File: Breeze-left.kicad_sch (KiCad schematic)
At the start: 102 parts, among them SW1 CHOCXHSPCB-1U, SW10 CHOCXHSPCB-1U, SW11 CHOCXHSPCB-1U, SW12 CHOCXHSPCB-1U, SW13 CHOCXHSPCB-1U, SW14 CHOCXHSPCB-1U, SW15 CHOCXHSPCB-1U, SW16 CHOCXHSPCB-1U, SW17 CHOCXHSPCB-1U, SW18 CHOCXHSPCB-1U, SW19 CHOCXHSPCB-1U, SW2 CHOCXHSPCB-1U, SW20 CHOCXHSPCB-1U, SW21 CHOCXHSPCB-1U, SW22 CHOCXHSPCB-1U, SW23 CHOCXHSPCB-1U, SW24 CHOCXHSPCB-1U, SW3 CHOCXHSPCB-1U, SW4 CHOCXHSPCB-1U, SW5 CHOCXHSPCB-1U, SW6 CHOCXHSPCB-1U, SW7 CHOCXHSPCB-1U, SW8 CHOCXHSPCB-1U, SW9 CHOCXHSPCB-1U

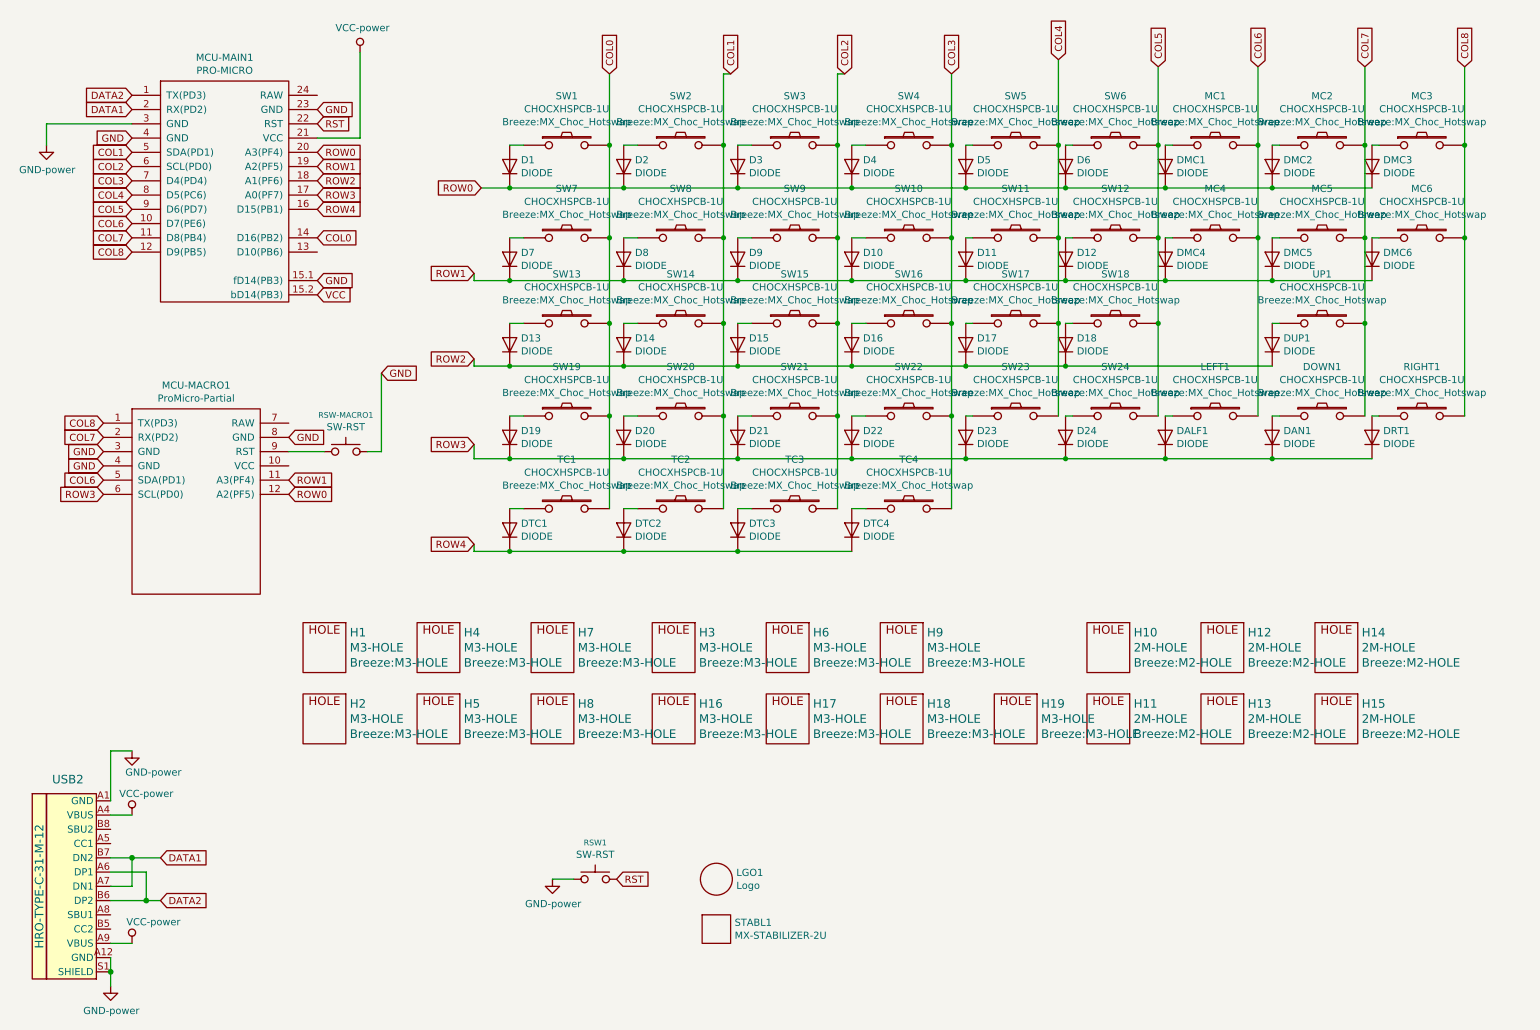
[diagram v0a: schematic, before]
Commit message: Copy right half to left
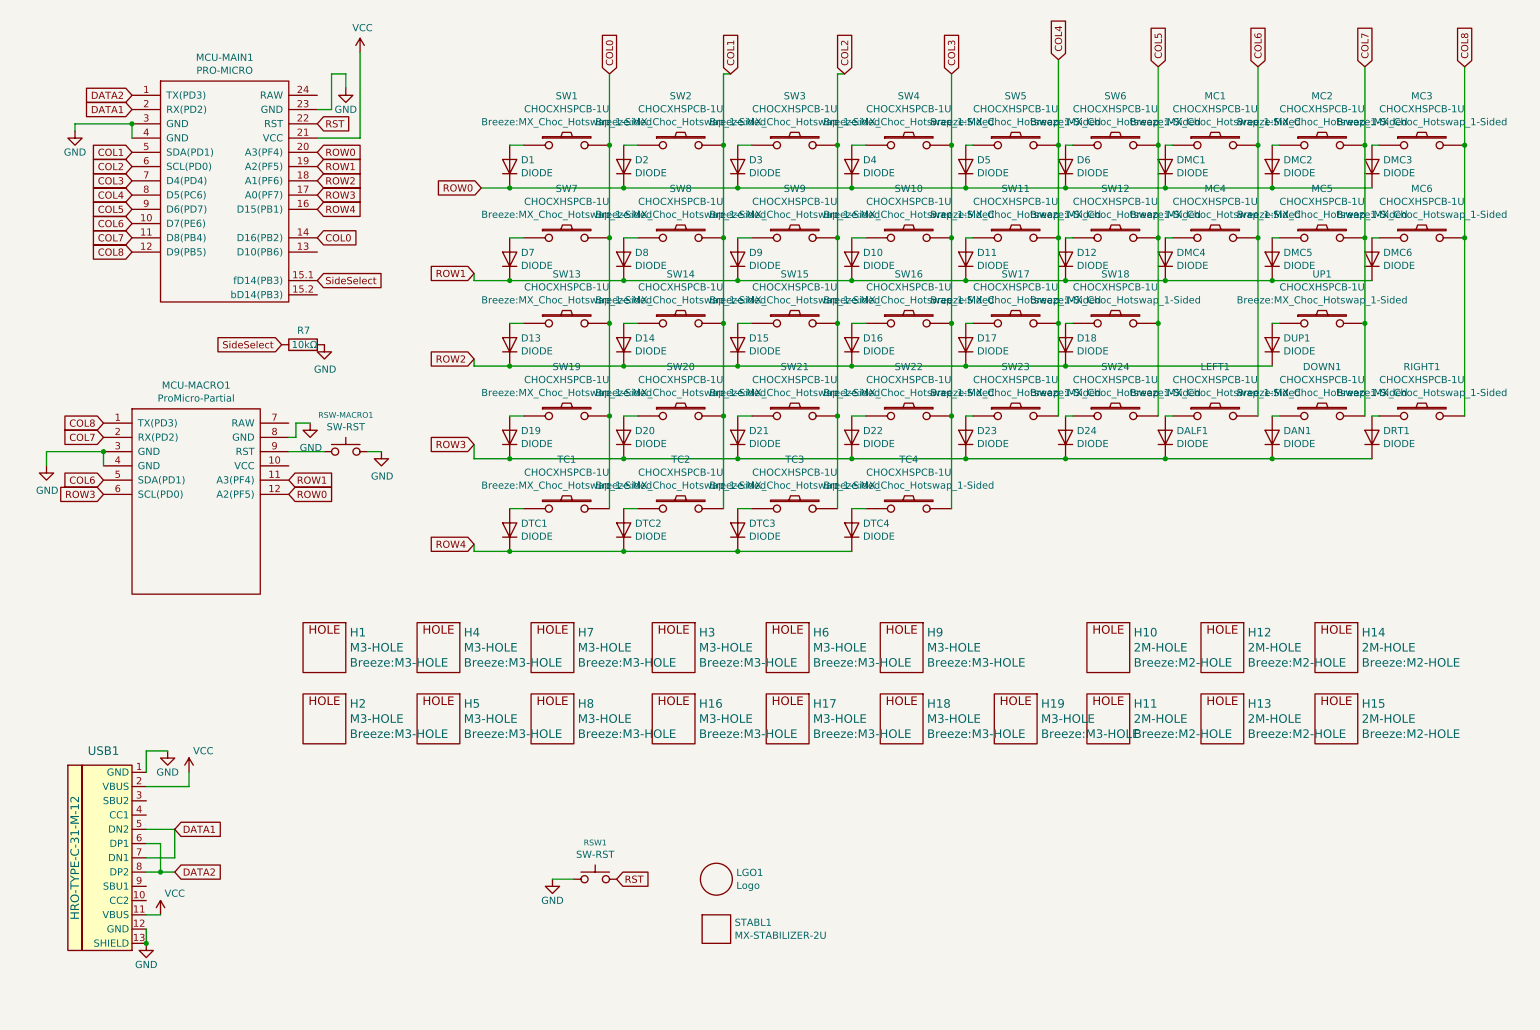
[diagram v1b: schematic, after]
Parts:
- removed USB2: HRO-TYPE-C-31-M-12, Connector_USB:USB_C_Receptacle_HRO_TYPE-C-31-M-12, symbol keebio:HRO-TYPE-C-31-M-12
- added R7: 10kΩ, Resistor_SMD:R_0603_1608Metric, symbol Device:R
- added USB1: HRO-TYPE-C-31-M-12, Keebio-Parts:USB-C-12-Pin-MidMount, symbol keebio:HRO-TYPE-C-31-M-12
- DOWN1, LEFT1, MC1, MC2, MC3, MC4, MC5, MC6, RIGHT1, SW1, SW10, SW11, SW12, SW13, SW14, SW15, SW16, SW17, SW18, SW19, SW2, SW20, SW21, SW22, SW23, SW24, SW3, SW4, SW5, SW6, SW7, SW8, SW9, TC1, TC2, TC3, TC4, UP1: footprint Breeze:MX_Choc_Hotswap -> Breeze:MX_Choc_Hotswap_1-Sided
- MCU-MAIN1: footprint Breeze:ProMicro -> Breeze:ProMicro_1-Sided
- RSW-MACRO1: footprint Breeze:TACT_SWITCH_TVBP06 -> Button_Switch_SMD:SW_SPST_TL3342
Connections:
- net DATA1: now also USB1.5 (DN2), USB1.7 (DN1)
- net DATA2: now also USB1.6 (DP1), USB1.8 (DP2)
- net GND: now also R7.2, USB1.1 (GND), USB1.12 (GND), USB1.13 (SHIELD); no longer MCU-MAIN1.15.1 (fD14(PB3))
- net VCC: now also USB1.11 (VBUS), USB1.2 (VBUS); no longer MCU-MAIN1.15.2 (bD14(PB3))
- new net SideSelect: MCU-MAIN1.15.1 (fD14(PB3)), R7.1

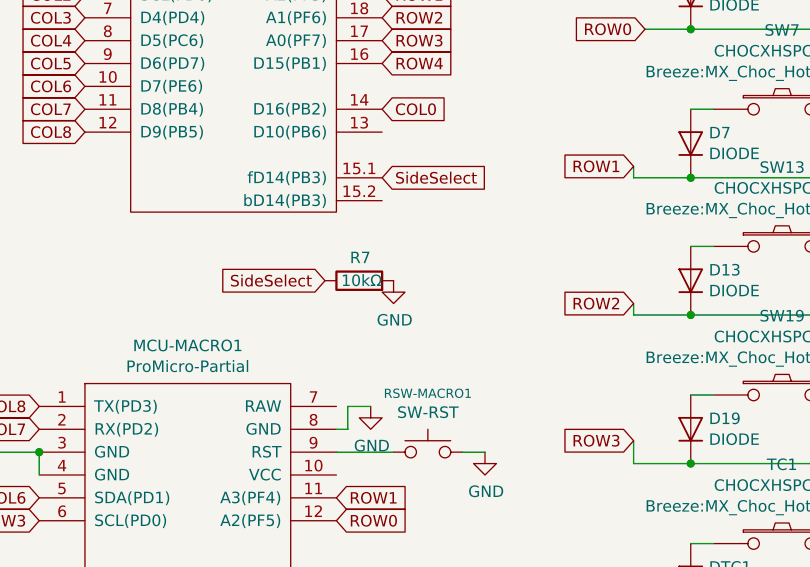
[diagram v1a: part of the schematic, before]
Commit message: Set side select config for left half
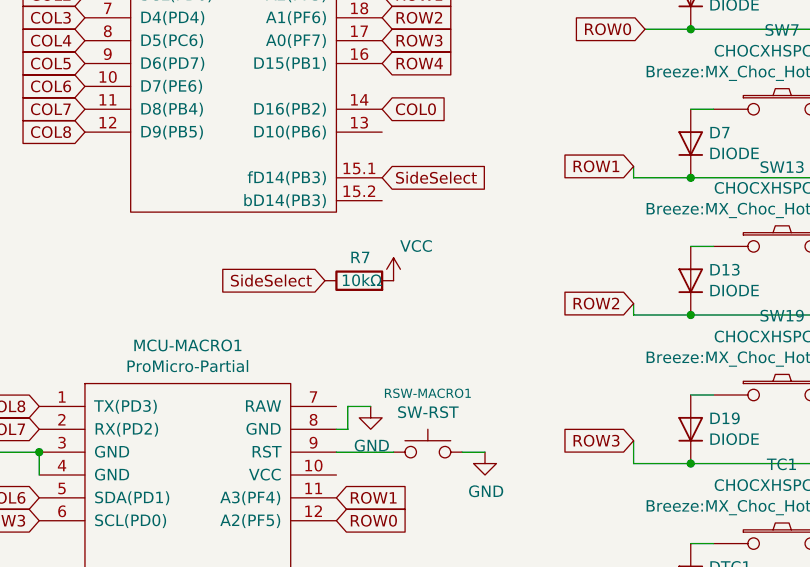
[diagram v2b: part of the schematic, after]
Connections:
- net GND: no longer R7.2
- net VCC: now also R7.2

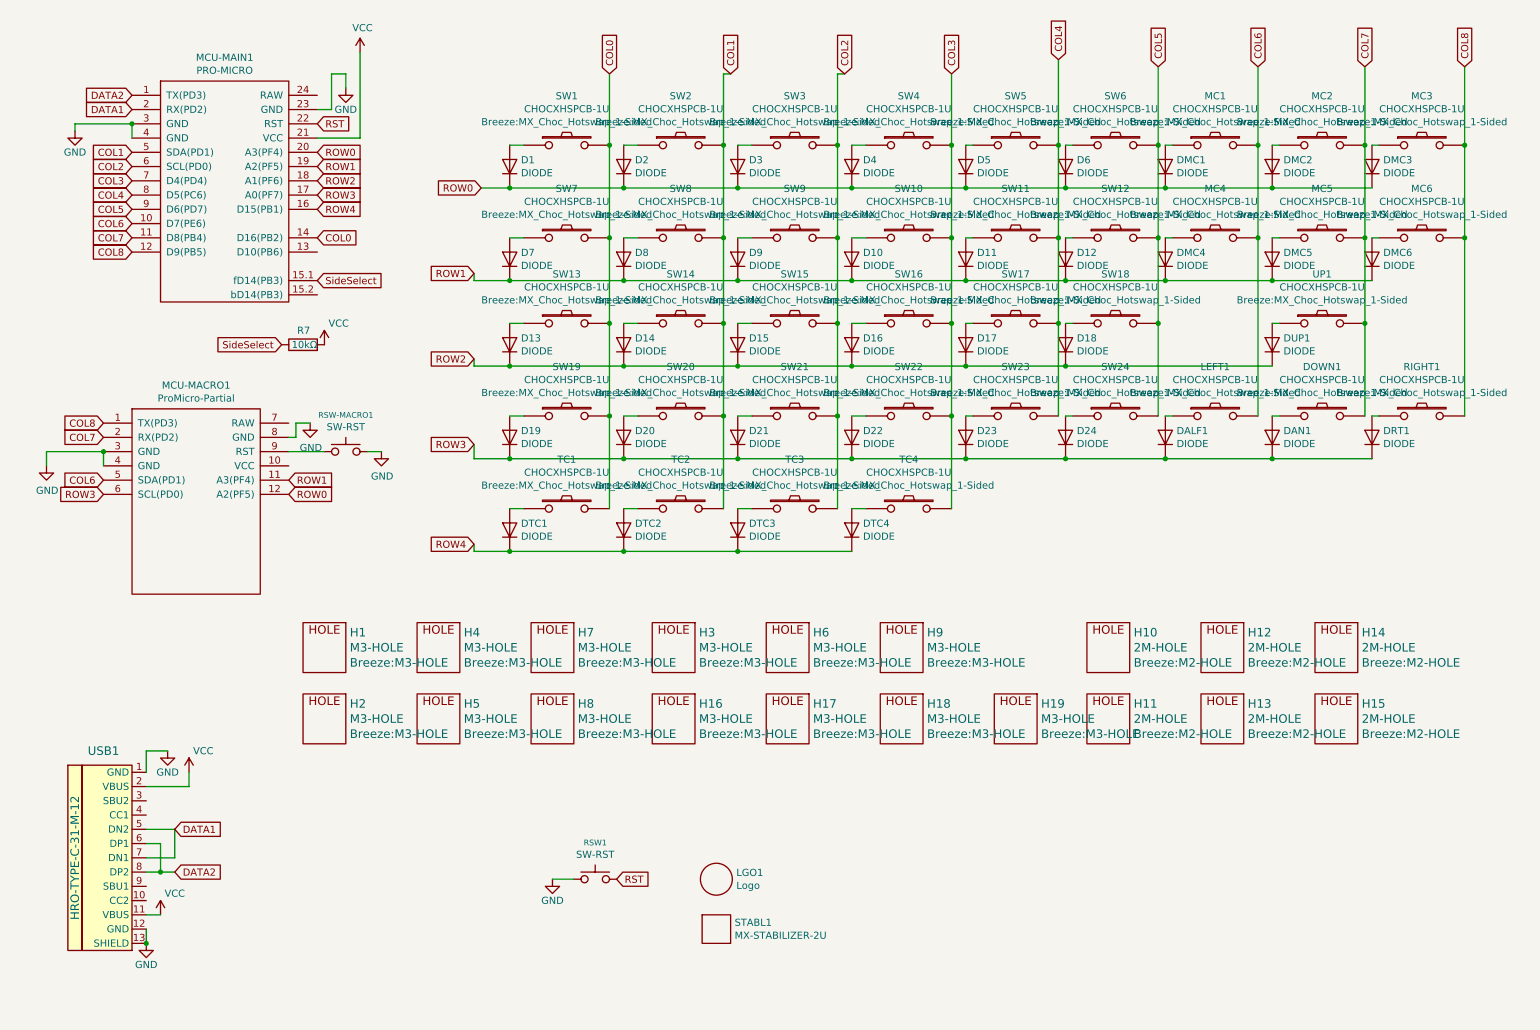
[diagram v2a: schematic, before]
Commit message: Remove extra holes and switches for breakoff portion on left half
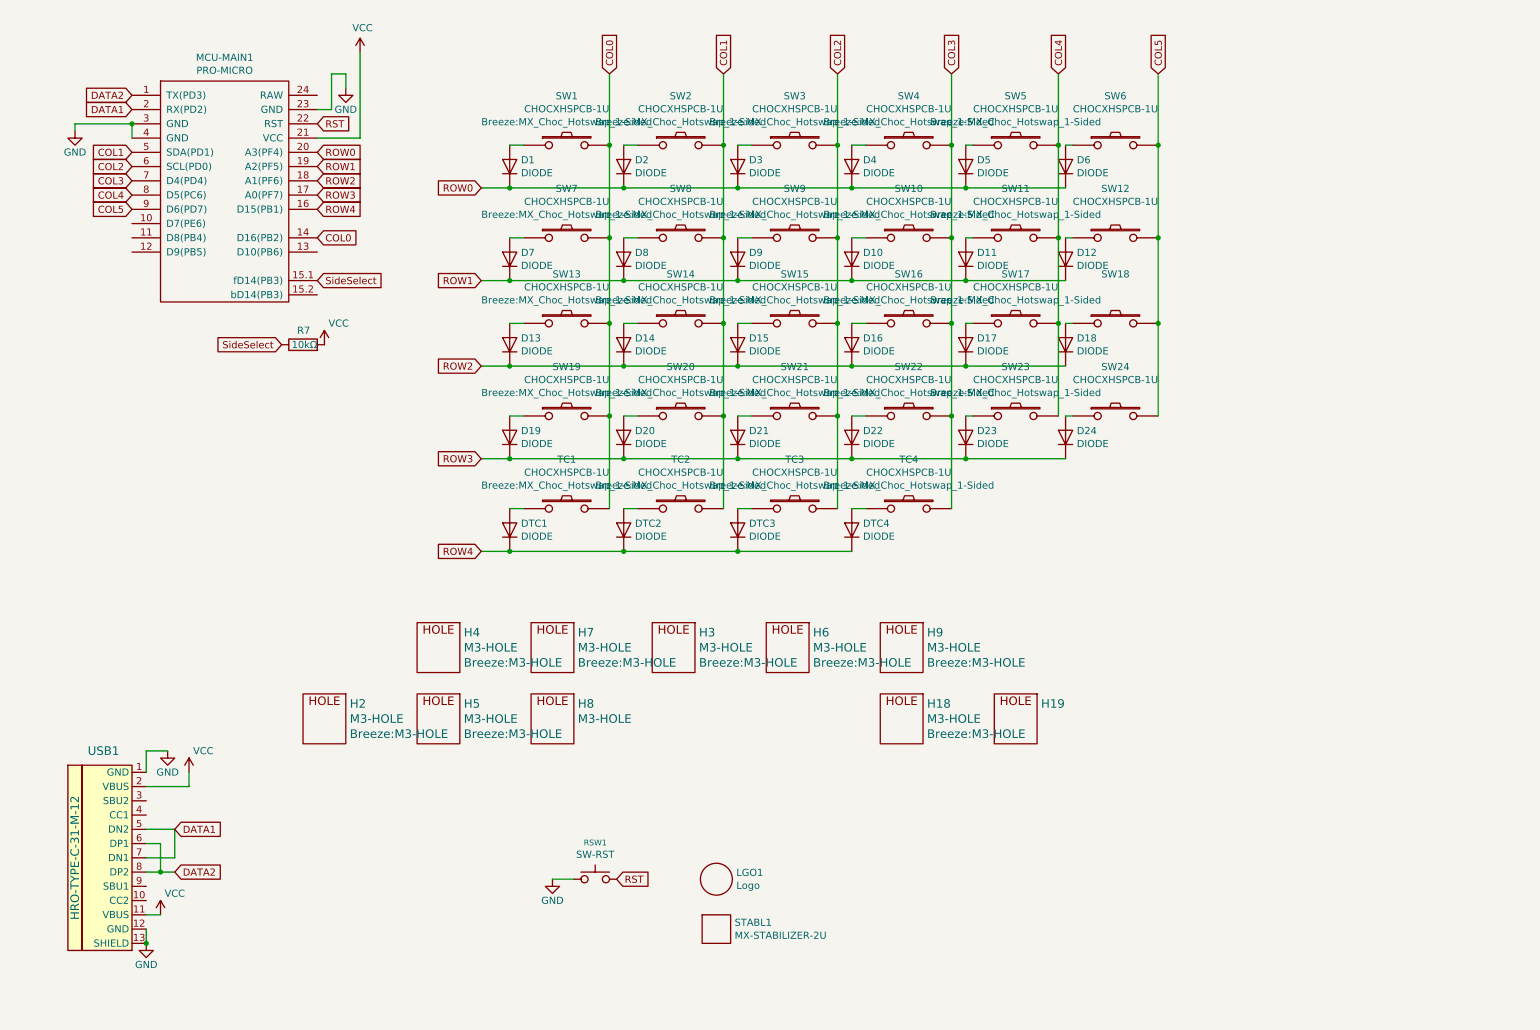
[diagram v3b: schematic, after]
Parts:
- removed DALF1, DAN1, DMC1, DMC2, DMC3, DMC4, DMC5, DMC6, DRT1, DUP1: DIODE, Breeze:SOD-123FL, symbol Breeze-rescue:Diode-cache-Merkaba_Rev0-rescue-Breeze-rescue
- removed DOWN1, LEFT1, MC1, MC2, MC3, MC4, MC5, MC6, RIGHT1, UP1: CHOCXHSPCB-1U, Breeze:MX_Choc_Hotswap_1-Sided, symbol Breeze-rescue:CHOCXHSPCB-1U-cache-Merkaba_Rev0-rescue-Breeze-rescue
- removed H1, H16, H17: M3-HOLE, Breeze:M3-HOLE, symbol Breeze-rescue:3M-HOLE-Merkaba_Rev0-rescue-Breeze-rescue
- removed H10, H11, H12, H13, H14, H15: 2M-HOLE, Breeze:M2-HOLE, symbol Breeze-rescue:2M-HOLE-Breeze-rescue
- removed MCU-MACRO1: ProMicro-Partial, Breeze:PROMICRO-PARTIAL2, symbol Breeze-rescue:ProMicro-Partial2-Merkaba_Rev0-rescue-Breeze-rescue
- removed RSW-MACRO1: SW-RST, Button_Switch_SMD:SW_SPST_TL3342, symbol Breeze-rescue:SW_RST-Lily58-cache-Merkaba_Rev0-rescue-Breeze-rescue
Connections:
- net COL6: no longer names the net of MCU-MAIN1.10 (D7(PE6))
- net COL7: no longer names the net of MCU-MAIN1.11 (D8(PB4))
- net COL8: no longer names the net of MCU-MAIN1.12 (D9(PB5))
